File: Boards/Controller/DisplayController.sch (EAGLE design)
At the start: 46 parts, among them J1 USB0001LF, J3 AVR_SPI_PRG_62X3_LOCK, Q1 BSS138, U1 MCP1703CB, U100 MCP73831, U101 MAX1797, U2 FT232RQ, U3 ATMEGA328P-MU, U5 MAX1704X, X2 CRYSTAL7A-20.000MAAJ-T

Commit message: added Rev Number (SVN 123) cosmetics
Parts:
- C100: NEWARK_PN (none) -> 48T2909
- J100: value (none) -> 38K8067
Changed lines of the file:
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@@
 <layer number="17" name="Pads" color="2" fill="1" visible="yes" active="no"/>
 <layer number="18" name="Vias" color="2" fill="1" visible="yes" active="no"/>
-<layer number="19" name="Unrouted" color="14" fill="1" visible="yes" active="no"/>
+<layer number="19" name="Unrouted" color="18" fill="1" visible="yes" active="no"/>
 <layer number="20" name="Dimension" color="15" fill="1" visible="yes" active="no"/>
 <layer number="21" name="tPlace" color="7" fill="1" visible="yes" active="no"/>
@@
 <part name="R1" library="SparkFun" deviceset="RESISTOR" device="0603-RES" value="330"/>
 <part name="GND18" library="SparkFun" deviceset="GND" device=""/>
-<part name="C100" library="SparkFun" deviceset="CAP" device="0603-CAP" value="4.7uF"/>
+<part name="C100" library="SparkFun" deviceset="CAP" device="0603-CAP" value="4.7uF">
+<attribute name="NEWARK_PN" value="48T2909"/>
+</part>
 <part name="GND19" library="SparkFun" deviceset="GND" device=""/>
-<part name="J100" library="SparkFun" deviceset="M02" device="-JST-2MM-SMT"/>
+<part name="J100" library="SparkFun" deviceset="M02" device="-JST-2MM-SMT" value="38K8067 "/>
 <part name="GND20" library="SparkFun" deviceset="GND" device=""/>
 <part name="R100" library="SparkFun" deviceset="RESISTOR" device="0805-RES" value="2K"/>
@@
 <instance part="R1" gate="G$1" x="93.98" y="149.86" rot="R180"/>
 <instance part="GND18" gate="1" x="121.92" y="152.4"/>
-<instance part="C100" gate="G$1" x="134.62" y="154.94"/>
+<instance part="C100" gate="G$1" x="134.62" y="154.94">
+<attribute name="NEWARK_PN" x="134.62" y="154.94" size="1.778" layer="96" display="off"/>
+</instance>
 <instance part="GND19" gate="1" x="134.62" y="147.32"/>
 <instance part="R100" gate="G$1" x="127" y="147.32" rot="R270"/>

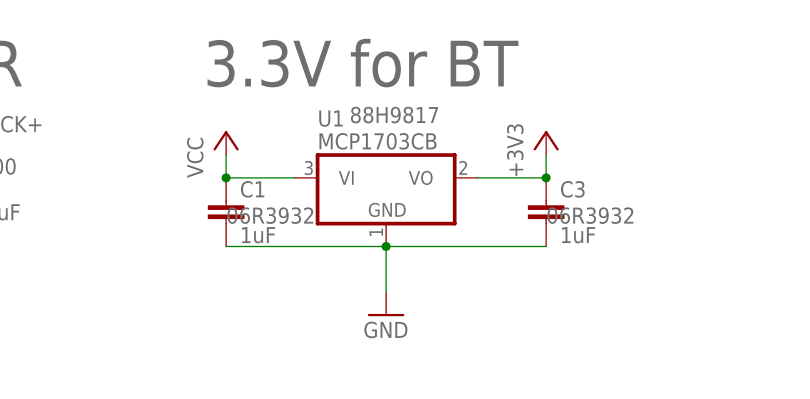
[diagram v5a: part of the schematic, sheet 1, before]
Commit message: Added Switch datasheets (a few alternates added that are drop in replacements) Added more Newark.com PN's to various parts
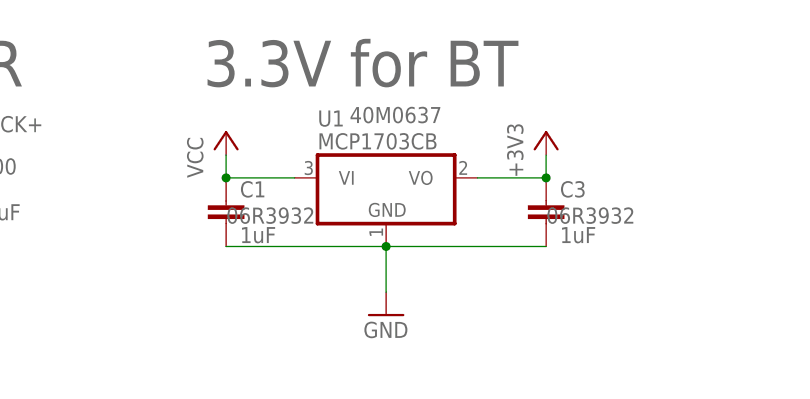
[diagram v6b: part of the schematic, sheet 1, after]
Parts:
- J1: NEWARK_PN (none) -> 82R7424
- U1: NEWARKPN 88H9817 -> 40M0637
- U100: NEWARK_PN (none) -> 56K7045
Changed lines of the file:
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@@
 <attribute name="OC_NEWARK" value="08N6809 "/>
 </part>
-<part name="U100" library="SparkFun" deviceset="MCP73831" device=""/>
+<part name="U100" library="SparkFun" deviceset="MCP73831" device="">
+<attribute name="NEWARK_PN" value="56K7045"/>
+</part>
 <part name="R1" library="SparkFun" deviceset="RESISTOR" device="0603-RES" value="330"/>
 <part name="GND18" library="SparkFun" deviceset="GND" device=""/>
@@
 <part name="U$2" library="MyParts" deviceset="DX_BT_MODULE" device=""/>
 <part name="U1" library="linear" deviceset="MCP1703" device="CB">
-<attribute name="NEWARKPN" value="88H9817 "/>
+<attribute name="NEWARKPN" value="40M0637"/>
 </part>
 <part name="Q1" library="transistor-small-signal" deviceset="BSS123" device="" value="BSS138">
@@
 <attribute name="OC_NEWARK" value="15M6870"/>
 </part>
-<part name="J1" library="MyParts" deviceset="USB" device="0001LF"/>
+<part name="J1" library="MyParts" deviceset="USB" device="0001LF">
+<attribute name="NEWARK_PN" value="82R7424"/>
+</part>
 <part name="C5" library="SparkFun" deviceset="CAP" device="0603-CAP" value="100nF"/>
 <part name="GND2" library="SparkFun" deviceset="GND" device=""/>
@@
 <instances>
 <instance part="GND16" gate="1" x="33.02" y="149.86"/>
-<instance part="U100" gate="G$1" x="109.22" y="160.02"/>
+<instance part="U100" gate="G$1" x="109.22" y="160.02">
+<attribute name="NEWARK_PN" x="109.22" y="160.02" size="1.778" layer="96" display="off"/>
+</instance>
 <instance part="R1" gate="G$1" x="93.98" y="149.86" rot="R180"/>
 <instance part="GND18" gate="1" x="121.92" y="152.4"/>
@@
 <instance part="P+1" gate="1" x="165.1" y="162.56"/>
 <instance part="+3V1" gate="G$1" x="200.66" y="162.56"/>
-<instance part="J1" gate="G$1" x="27.94" y="162.56" rot="R180"/>
+<instance part="J1" gate="G$1" x="27.94" y="162.56" rot="R180">
+<attribute name="NEWARK_PN" x="27.94" y="162.56" size="1.778" layer="96" rot="R180" display="off"/>
+</instance>
 <instance part="U101" gate="G$1" x="187.96" y="93.98"/>
 <instance part="GND23" gate="1" x="187.96" y="76.2"/>

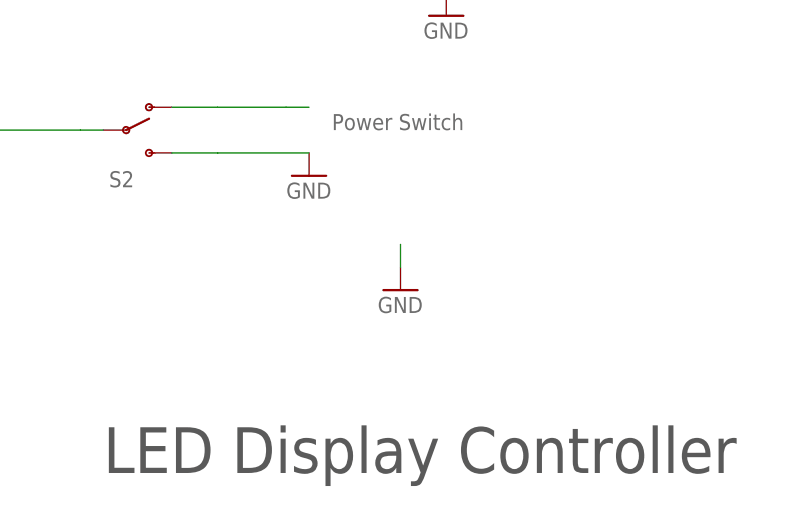
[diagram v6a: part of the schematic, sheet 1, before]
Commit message: removed stray ground symbol that was a copy never used.
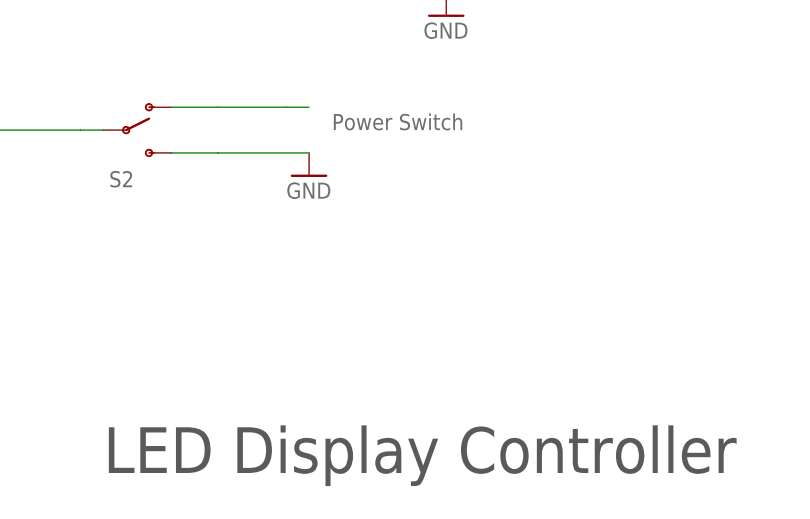
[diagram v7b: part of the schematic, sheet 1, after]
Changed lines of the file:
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@@
 <part name="S2" library="SparkFun-Electromechanical" deviceset="SWITCH-SPDT" device="-SMD-A"/>
 <part name="GND15" library="SparkFun" deviceset="GND" device=""/>
-<part name="GND17" library="SparkFun" deviceset="GND" device=""/>
 <part name="U$1" library="MyParts" deviceset="IFSC" device="1515AHER220M01">
 <attribute name="NEWARK_PN" value="47T5127"/>
@@
 <instance part="S2" gate="1" x="152.4" y="63.5"/>
 <instance part="GND15" gate="1" x="172.72" y="58.42"/>
-<instance part="GND17" gate="1" x="182.88" y="45.72"/>
 <instance part="U$1" gate="G$1" x="185.674" y="111.76">
 <attribute name="NEWARK_PN" x="185.674" y="111.76" size="1.778" layer="96"/>
@@
 <pinref part="GND15" gate="1" pin="GND"/>
 </segment>
-<segment>
-<pinref part="GND17" gate="1" pin="GND"/>
-<wire x1="182.88" y1="48.26" x2="182.88" y2="50.8" width="0.1524" layer="91"/>
-</segment>
 </net>

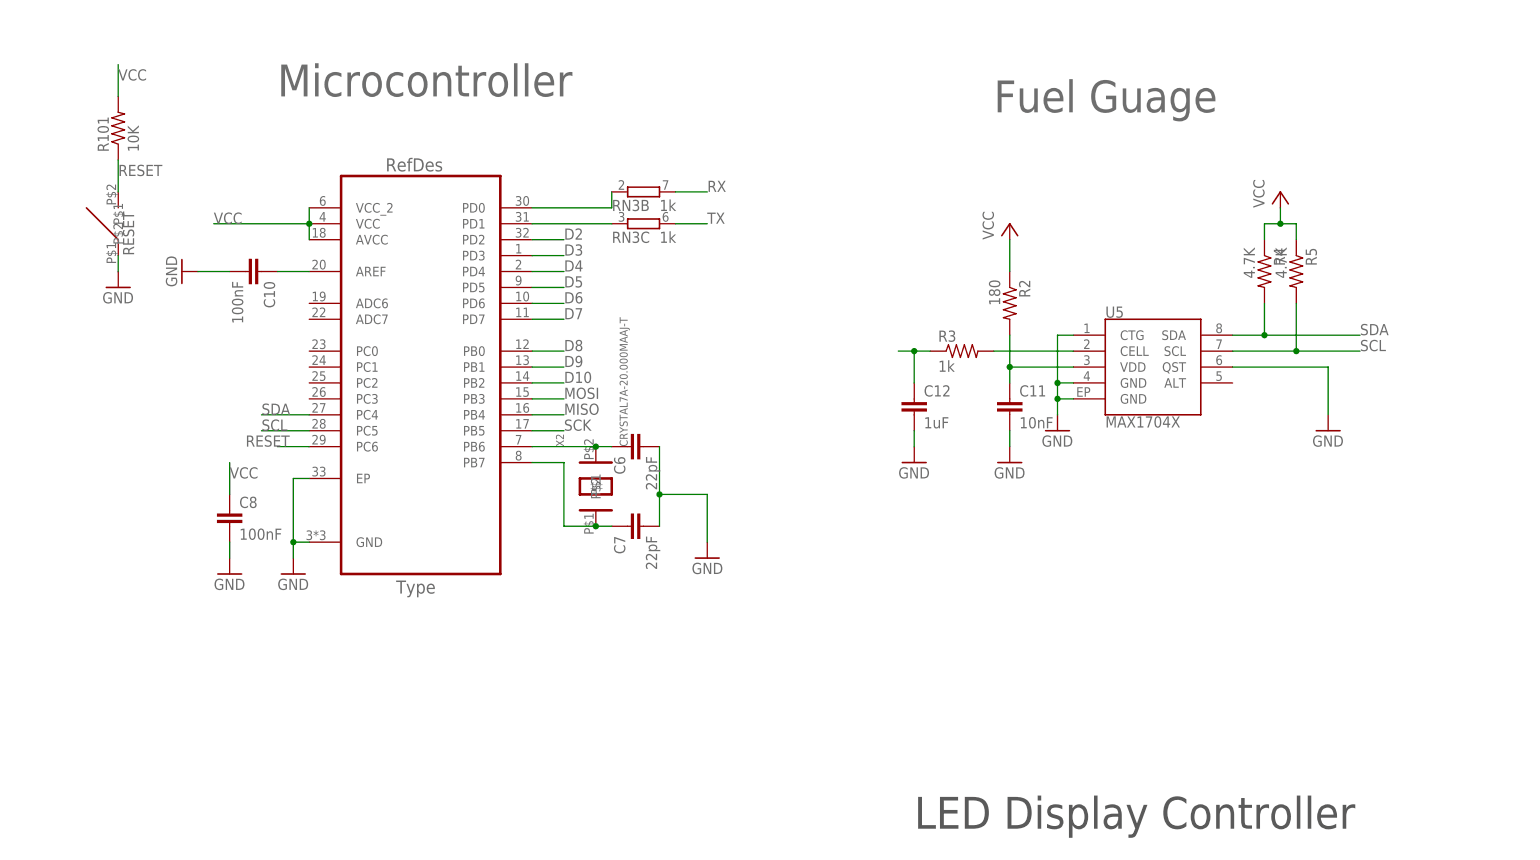
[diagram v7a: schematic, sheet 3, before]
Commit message: Fixed bottom ground plane being .2mm above outline Cleaned up traces a bit Added 100uF cap to top power pin of atmega328p (all power pins now have a cap) Added 10k resistor to BT module reset line (to hold it high)
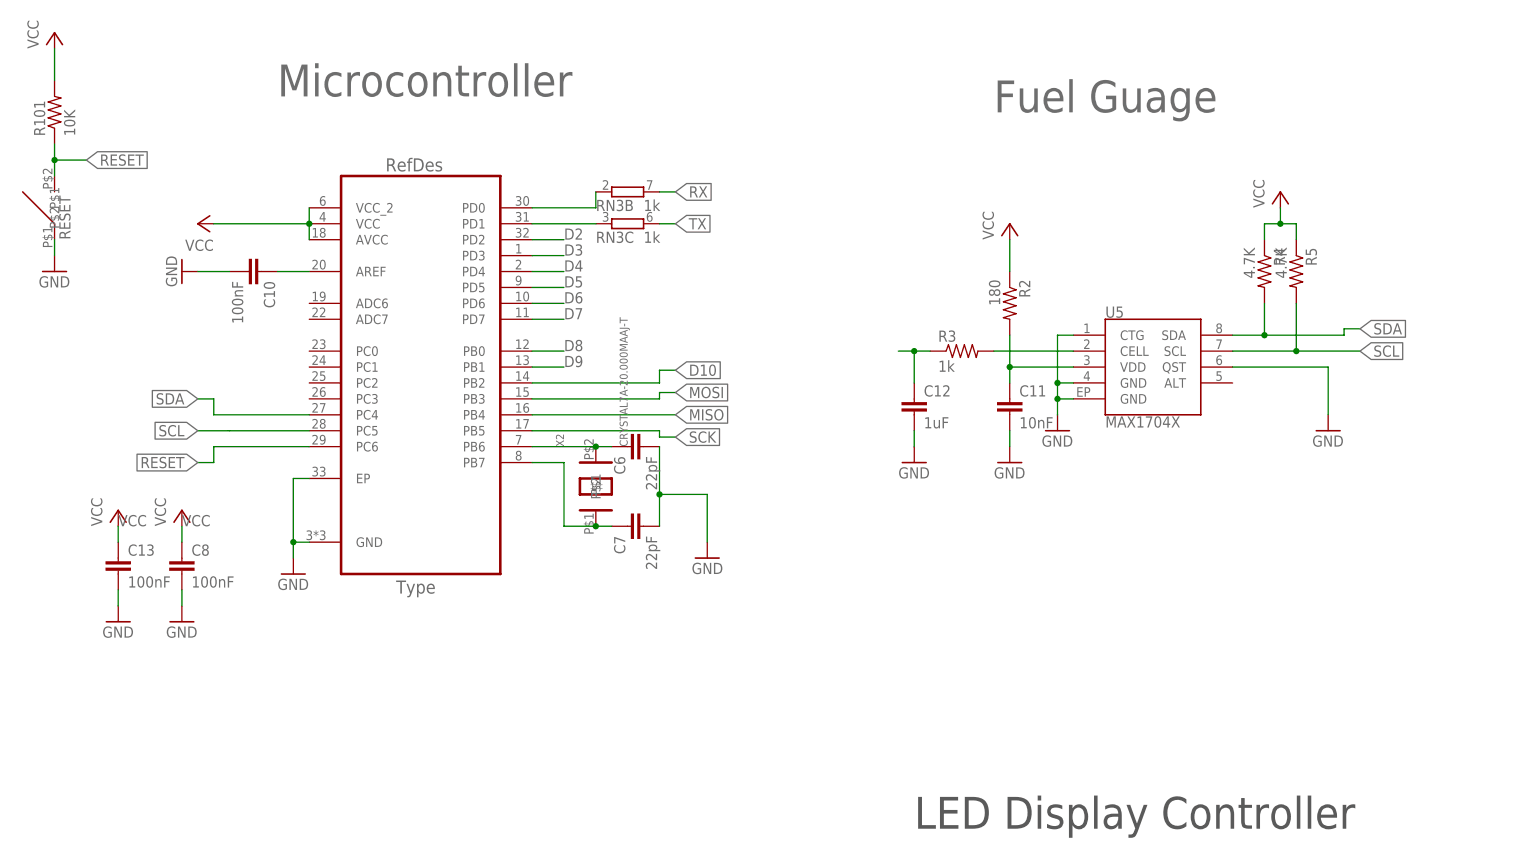
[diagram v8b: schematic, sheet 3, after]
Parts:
- removed TP1: TPSQTP14SQ, testpad:TPSQTP14SQ
- added C13: 100nF, SparkFun:CAP0603-CAP
- added R7: 10k, SparkFun:RESISTOR0603-RES
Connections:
- new net BTRESET: R7.1, U$2.RESET
- net +3V3: now also R7.2; no longer U$2.RESET
- net GND: now also C13.2
- net VCC: now also C13.1; no longer TP1.TP
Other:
- moved on the sheet: C8, R101, RN3B, RN3C
